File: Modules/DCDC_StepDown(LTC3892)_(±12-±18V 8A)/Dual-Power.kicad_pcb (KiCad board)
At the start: 4 copper layers, 58.4 x 55.9 mm, 81 parts, among them J1 Conn_02x05_Top_Bottom, J2 Conn_02x05_Top_Bottom, J3 Conn_01x02, Q1 BSC028N06LS3, Q2 BSC028N06LS3, Q3 BSC028N06LS3, Q4 BSC028N06LS3, Q5 BSC028N06LS3, U1 LTC3892EUHPBF, U2 LT1797

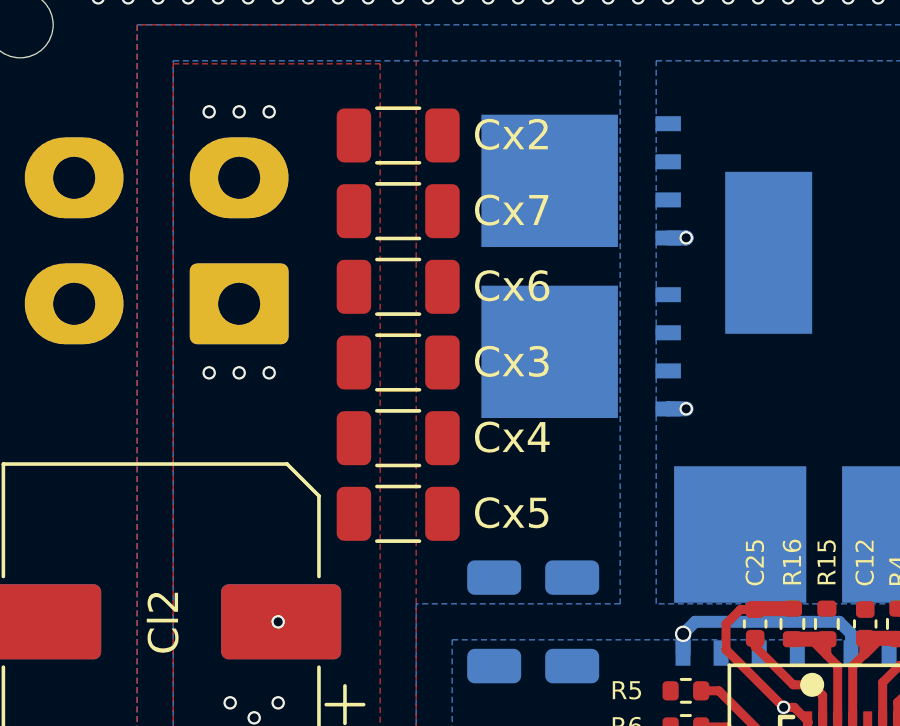
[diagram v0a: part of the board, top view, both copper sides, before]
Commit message: update Dual-Power components value
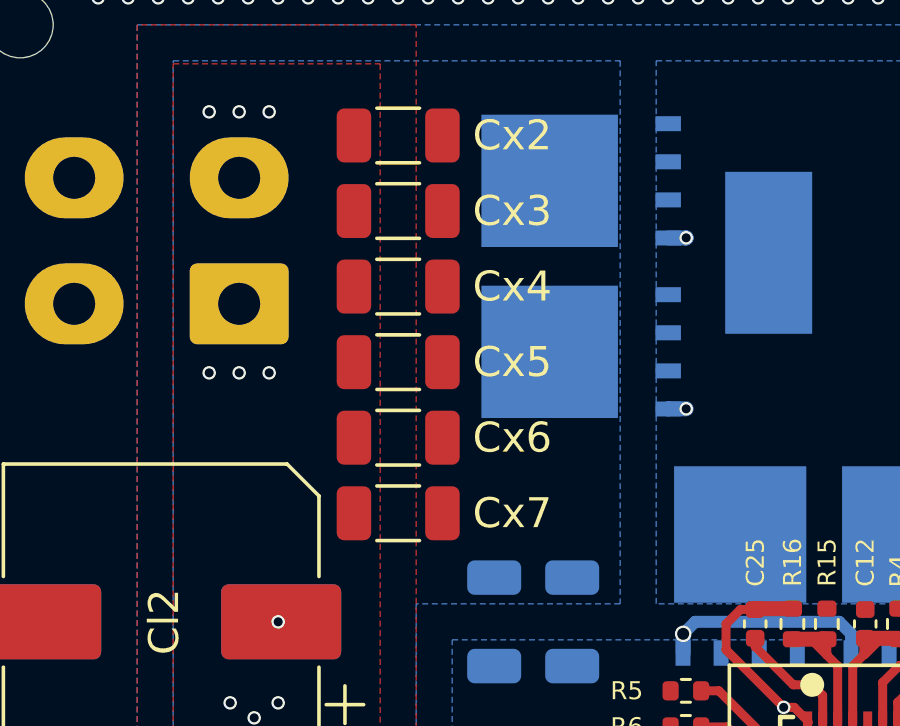
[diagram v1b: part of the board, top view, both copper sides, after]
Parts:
- moved Cx7 10.1 mm to (127.4, 77.9)
- moved Cx5 5.06 mm to (127.4, 72.8)
- moved Cx4 5.05 mm to (127.4, 70.3)
- moved Cx3 5.05 mm to (127.4, 67.8)
- moved Cx6 5.03 mm to (127.4, 75.4)
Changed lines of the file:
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@@
   )
   (footprint "Capacitor_SMD:C_1206_3216Metric" (layer "F.Cu")
-    (at 127.4 72.855554 180)
+    (at 127.4 67.807332 180)
     (descr "Capacitor SMD 1206 (3216 Metric), square (rectangular) end terminal, IPC_7351 nominal, (Body size source: IPC-SM-782 page 76, https://www.pcb-3d.com/wordpress/wp-content/uploads/ipc-sm-782a_amendment_1_and_2.pdf), generated with kicad-footprint-generator")
     (tags "capacitor")
@@
   )
   (footprint "Capacitor_SMD:C_1206_3216Metric" (layer "F.Cu")
-    (at 127.4 75.377776 180)
+    (at 127.4 70.325776 180)
     (descr "Capacitor SMD 1206 (3216 Metric), square (rectangular) end terminal, IPC_7351 nominal, (Body size source: IPC-SM-782 page 76, https://www.pcb-3d.com/wordpress/wp-content/uploads/ipc-sm-782a_amendment_1_and_2.pdf), generated with kicad-footprint-generator")
     (tags "capacitor")
@@
   )
   (footprint "Capacitor_SMD:C_1206_3216Metric" (layer "F.Cu")
-    (at 127.4 77.9 180)
+    (at 127.4 72.84422 180)
     (descr "Capacitor SMD 1206 (3216 Metric), square (rectangular) end terminal, IPC_7351 nominal, (Body size source: IPC-SM-782 page 76, https://www.pcb-3d.com/wordpress/wp-content/uploads/ipc-sm-782a_amendment_1_and_2.pdf), generated with kicad-footprint-generator")
     (tags "capacitor")
@@
   )
   (footprint "Capacitor_SMD:C_1206_3216Metric" (layer "F.Cu")
-    (at 127.4 70.333332 180)
+    (at 127.4 75.362664 180)
     (descr "Capacitor SMD 1206 (3216 Metric), square (rectangular) end terminal, IPC_7351 nominal, (Body size source: IPC-SM-782 page 76, https://www.pcb-3d.com/wordpress/wp-content/uploads/ipc-sm-782a_amendment_1_and_2.pdf), generated with kicad-footprint-generator")
     (tags "capacitor")
@@
   )
   (footprint "Capacitor_SMD:C_1206_3216Metric" (layer "F.Cu")
-    (at 127.4 67.81111 180)
+    (at 127.4 77.88111 180)
     (descr "Capacitor SMD 1206 (3216 Metric), square (rectangular) end terminal, IPC_7351 nominal, (Body size source: IPC-SM-782 page 76, https://www.pcb-3d.com/wordpress/wp-content/uploads/ipc-sm-782a_amendment_1_and_2.pdf), generated with kicad-footprint-generator")
     (tags "capacitor")
